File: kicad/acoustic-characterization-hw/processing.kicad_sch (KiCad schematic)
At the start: 22 parts, among them IC1 ECP5-BGA256, J2 Conn_01x04_Socket, J4 Conn_01x06_Socket, U4 W25Q128JVS

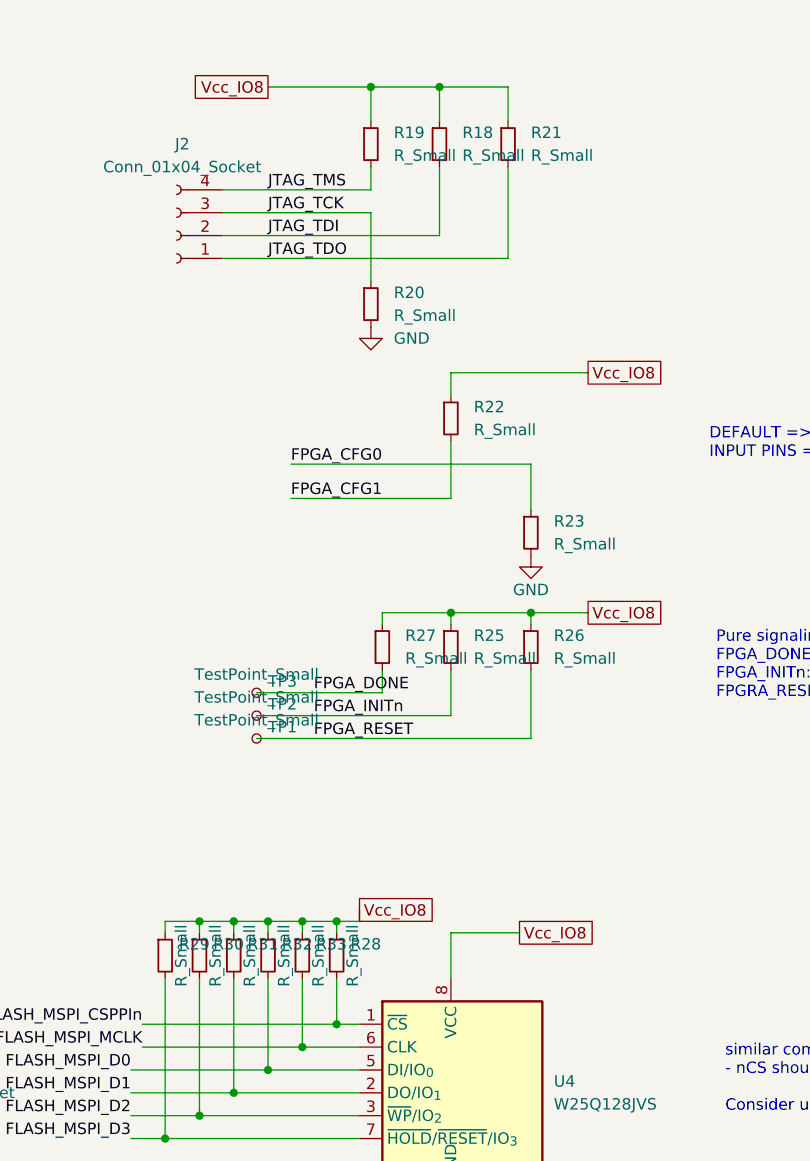
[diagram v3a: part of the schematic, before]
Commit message: [kicad] re-added passive values after accidental removal
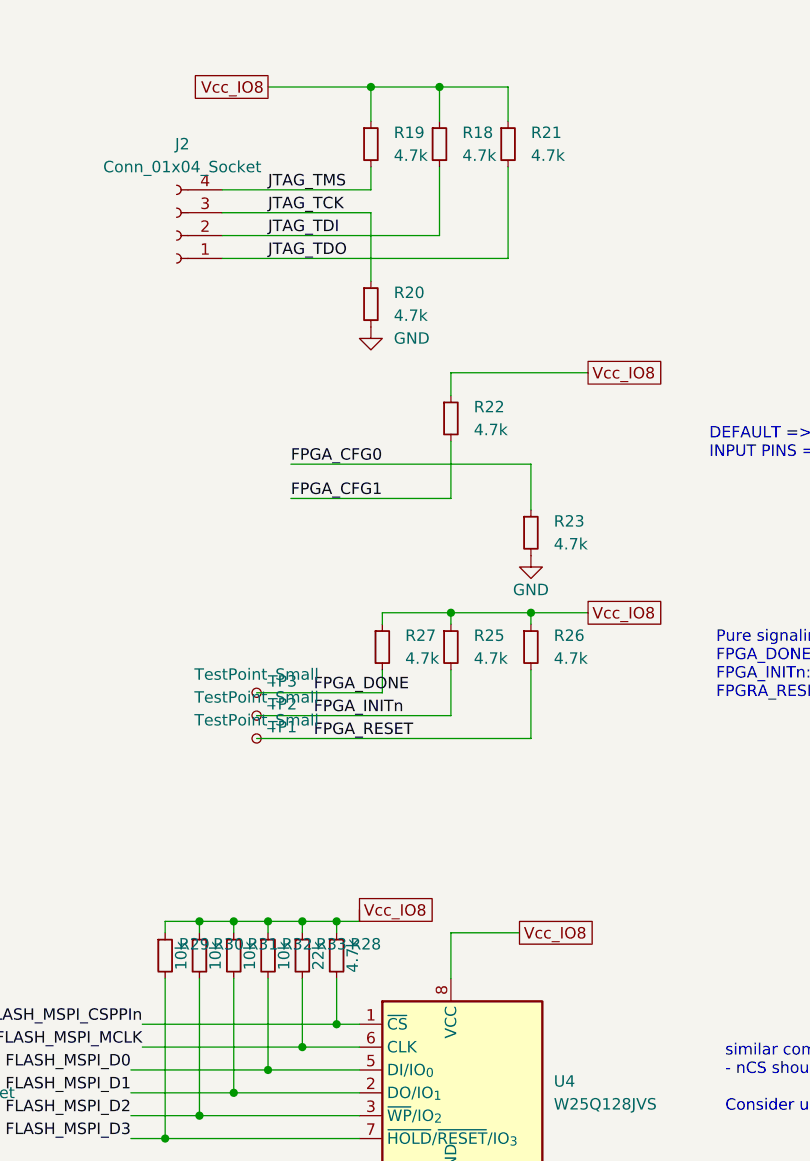
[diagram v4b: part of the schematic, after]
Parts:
- R18, R19, R20, R21, R22, R23, R25, R26, R27, R28: value R_Small -> 4.7k
- R29, R30, R31, R32: value R_Small -> 10k
- R33: value R_Small -> 22k
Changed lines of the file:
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@@
 			)
 		)
-		(property "Value" "R_Small"
+		(property "Value" "4.7k"
 			(at 261.62 90.1699 0)
 			(effects
@@
 			)
 		)
-		(property "Value" "R_Small"
+		(property "Value" "4.7k"
 			(at 270.51 90.1699 0)
 			(effects
@@
 			)
 		)
-		(property "Value" "R_Small"
+		(property "Value" "4.7k"
 			(at 254 90.1699 0)
 			(effects
@@
 			)
 		)
-		(property "Value" "R_Small"
+		(property "Value" "4.7k"
 			(at 261.62 64.7699 0)
 			(effects
@@
 			)
 		)
-		(property "Value" "R_Small"
+		(property "Value" "10k"
 			(at 236.728 123.19 90)
 			(effects
@@
 			)
 		)
-		(property "Value" "R_Small"
+		(property "Value" "4.7k"
 			(at 248.158 123.19 90)
 			(effects
@@
 			)
 		)
-		(property "Value" "R_Small"
+		(property "Value" "4.7k"
 			(at 252.73 52.0699 0)
 			(effects
@@
 			)
 		)
-		(property "Value" "R_Small"
+		(property "Value" "4.7k"
 			(at 260.35 34.2899 0)
 			(effects
@@
 			)
 		)
-		(property "Value" "R_Small"
+		(property "Value" "10k"
 			(at 232.918 123.19 90)
 			(effects
@@
 			)
 		)
-		(property "Value" "R_Small"
+		(property "Value" "22k"
 			(at 244.348 123.19 90)
 			(effects
@@
 			)
 		)
-		(property "Value" "R_Small"
+		(property "Value" "10k"
 			(at 229.108 123.19 90)
 			(effects
@@
 			)
 		)
-		(property "Value" "R_Small"
+		(property "Value" "10k"
 			(at 240.538 123.19 90)
 			(effects
@@
 			)
 		)
-		(property "Value" "R_Small"
+		(property "Value" "4.7k"
 			(at 267.97 34.2899 0)
 			(effects
@@
 			)
 		)
-		(property "Value" "R_Small"
+		(property "Value" "4.7k"
 			(at 252.73 34.2899 0)
 			(effects
@@
 			)
 		)
-		(property "Value" "R_Small"
+		(property "Value" "4.7k"
 			(at 270.51 77.4699 0)
 			(effects
